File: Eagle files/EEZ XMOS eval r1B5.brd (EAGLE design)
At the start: 100 x 85 mm, 228 parts, among them IC1 TPS61169DCKR, IC10 IS42S16400J, IC11 SN74CBTLV3257, IC12 SN74LVC1G02DBVR, IC13 AT25SF041-SSHDT, IC14 SN74CBTLV3257, IC15 TPS2051BDBVR, IC16 TPD2E001DZDR, IC17 TPS561208DDCR, IC18 XE216-512-TQ128-C20, IC19 TPD4E001DRLR, IC2 TPS561208DDCR, IC20 TPD4E001DRLR, IC21 74LVC1G07SE-7, IC22 74LVC1G07SE-7, IC23 TPA6205A1DGN, IC24 DP83848CVV/NOPB, IC26 74VHC595MTC, IC27 PCA21125T/Q900/1,1, IC28 MCP23S17-E/SS, IC29 M95256-WMN6P, IC3 74VHC595MTC, IC4 TPS561208DDCR, IC5 74VHC595MTC, IC6 TPS3808G33DBVR, IC7 AR1021-I/SS, IC8 TPS3808G09DBVR, IC9 74AUP1G74DC.125, J1 678038020, J2 5033981892, Q1 IRLML2246TRPBF, SW1 1301.9316, X1 FC68149, X2 SSW-105-02-S-D, X3 TSW-104-02-S-D_NN, X4 TSW-103-07-F-D, X5 ZL231-20KG, X6 22-23-2021, X7 LMJTAB881243M-L, X8 SSW-107-02-S-D, X9 PCA-6G-20-HL-3 or 52746-2071, Y1 XTAL016178- 85SMX

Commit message: #1, #2
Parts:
- D1: value (none) -> NSR0240
- R13: device rcl:R1206 -> rcl:R0805
- R14, R24: value 10K -> 1K
- R23: value 56K -> 5K6
- R4: value 34K -> 15K
- R6: value 10K -> 4K7
- R67: value 0R -> N.C.
- R8: value 5K1 -> 2K7
- R9: value 16K -> 10K
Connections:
- removed net 3: X1.3
- net +3V3: now also X2.3
- net GND: now also X1.3; no longer X2.3
- net N$35: now also IC9.5; no longer IC9.3
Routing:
- net N$35: track 39.1 -> 36.1 mm
- net GND: track 258.5 -> 259.9 mm
- net N$78: track 2.72 -> 2.16 mm
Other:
- board text added: "(max."
- board text added: "16V)"
- board text added: "EEZ XMOS evaluation board (02/2018 r1B5)"
- board text removed: "(max. 16V)"
- board text removed: "EEZ XMOS evaluation board (01/2018 r1B4)"

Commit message: #3
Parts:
- removed ZD1: BZX384-B30.115, EEZ_Lib1:SOD323-W
- added C82: 2u2, rcl:C0805
- added JP1: 0R-JUMPA, jump-0r-smd:A0R-JMP
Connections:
- new net N$24: JP1.2, LCD1.36
- net !RESET: now also JP1.1; no longer LCD1.36
- net +3V3: now also C82.1
- net GND: now also C82.2, JP1.3
- net VLED+: no longer ZD1.C
- net VLED-: no longer ZD1.A
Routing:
- net N$24: track 0.00 -> 5.82 mm
- net !RESET: track 141.3 -> 136.3 mm
- net GND: track 259.9 -> 262.4 mm, vias 198 -> 200
- net +3V3: track 175.9 -> 178.2 mm
- net VLED-: track 15.0 -> 14.1 mm
- net VLED+: track 2.92 -> 3.82 mm
- net N$2: track 11.6 -> 10.9 mm
- net LCD_VSYNC: track 40.2 -> 39.4 mm

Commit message: fixed flash memory model
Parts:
- IC13: value AT25SF041-SSHDT -> AT25SF081-SSHDT
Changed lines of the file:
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@@
 <attribute name="NAME" x="50.975" y="74.1765" size="1.016" layer="25" ratio="10"/>
 </element>
-<element name="IC13" library="EEZ_Lib1" package="SOIC127P600X175-8N" value="AT25SF041-SSHDT" x="58.674" y="29.718" smashed="yes" rot="R270">
+<element name="IC13" library="EEZ_Lib1" package="SOIC127P600X175-8N" value="AT25SF081-SSHDT" x="58.674" y="29.718" smashed="yes" rot="R270">
 <attribute name="NAME" x="57.8866" y="33.528" size="1.016" layer="25" ratio="10" rot="SR0"/>
 <attribute name="VALUE" x="53.5686" y="29.337" size="0.6096" layer="27" ratio="10" rot="SR0"/>
@@
 </signal>
 </signals>
-<errors>
-</errors>
 </board>
 </drawing>

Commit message: #6
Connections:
- net !SPI0_TOUCH renamed !SPI1_TOUCH
- removed net N$4: C15.1, IC7.16, LCD1.38, R11.2
- new net N$53: C15.1, IC7.16, LCD1.38
- net +3V3: now also IC7.2
- net GND: now also IC7.4; no longer IC7.2
- net N$3: now also R11.2
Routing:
- net N$4: track 29.4 -> 0.00 mm, vias 3 -> 0
- net N$53: track 0.00 -> 19.7 mm, vias 0 -> 2
- net N$3: track 15.1 -> 23.1 mm, vias 0 -> 2
- net N$8: track 6.85 -> 7.50 mm
- net +3V3: track 178.2 -> 178.9 mm
- net !RESET: track 136.3 -> 135.7 mm
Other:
- board text added: "EEZ XMOS evaluation board (04/2018 r1B5)"
- board text removed: "EEZ XMOS evaluation board (02/2018 r1B5)"

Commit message: #7
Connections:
- net +3V3: now also R51.1, R52.1
- net GND: no longer R51.1, R52.1
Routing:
- net +3V3: track 178.9 -> 181.8 mm, vias 69 -> 70
- net GND: track 262.4 -> 259.5 mm, vias 200 -> 199
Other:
- board text added: "EEZ XMOS evaluation board (05/2018 r1B5)"
- board text removed: "EEZ XMOS evaluation board (04/2018 r1B5)"
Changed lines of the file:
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@@
 <layer number="21" name="tPlace" color="7" fill="1" visible="yes" active="yes"/>
 <layer number="22" name="bPlace" color="3" fill="1" visible="no" active="yes"/>
-<layer number="23" name="tOrigins" color="15" fill="1" visible="no" active="yes"/>
+<layer number="23" name="tOrigins" color="15" fill="1" visible="yes" active="yes"/>
 <layer number="24" name="bOrigins" color="15" fill="1" visible="no" active="yes"/>
 <layer number="25" name="tNames" color="7" fill="1" visible="yes" active="yes"/>
@@
 <rectangle x1="95.9784" y1="77.4253" x2="96.3784" y2="77.4291" layer="21"/>
 <rectangle x1="96.0317" y1="77.4291" x2="96.2717" y2="77.4329" layer="21"/>
-<text x="99.1275" y="15.2085" size="1.016" layer="21" font="vector" ratio="10" rot="SR90">EEZ XMOS evaluation board (04/2018 r1B5)</text>
-<text x="1.5875" y="23.241" size="1.016" layer="16" ratio="10" rot="SMR90">EEZ XMOS evaluation board (04/2018 r1B5)</text>
+<text x="99.1275" y="15.2085" size="1.016" layer="21" font="vector" ratio="10" rot="SR90">EEZ XMOS evaluation board (05/2018 r1B5)</text>
+<text x="1.5875" y="23.241" size="1.016" layer="16" ratio="10" rot="SMR90">EEZ XMOS evaluation board (05/2018 r1B5)</text>
 <wire x1="100" y1="83.5" x2="100" y2="1.5" width="0.1" layer="20"/>
 <dimension x1="0" y1="-2" x2="100" y2="-3.5" x3="50" y3="-7" layer="47" dtype="horizontal"/>
@@
 <contactref element="C71" pad="-"/>
 <contactref element="C72" pad="2"/>
-<contactref element="R52" pad="1"/>
-<contactref element="R51" pad="1"/>
 <contactref element="IC24" pad="35"/>
 <contactref element="IC24" pad="47"/>
@@
 <wire x1="56.0705" y1="63.6905" x2="56.8842" y2="63.881" width="0.2032" layer="1"/>
 <wire x1="56.8842" y1="63.881" x2="56.9096" y2="63.8556" width="0.2032" layer="1"/>
-<via x="73.406" y="73.152" extent="1-16" drill="0.3" shape="square"/>
 <via x="55.372" y="58.674" extent="1-16" drill="0.3" shape="square"/>
 <wire x1="64.262" y1="69.472" x2="64.262" y2="70.5485" width="0.254" layer="1"/>
@@
 <wire x1="59.563" y1="53.975" x2="59.563" y2="53.2647" width="0.254" layer="1"/>
 <wire x1="59.563" y1="53.2647" x2="59.5766" y2="53.2511" width="0.254" layer="1"/>
-<wire x1="71.4629" y1="72.2351" x2="73.4314" y2="72.2351" width="0.254" layer="1"/>
-<wire x1="73.4314" y1="72.2351" x2="73.4314" y2="73.1266" width="0.254" layer="1"/>
-<wire x1="73.4314" y1="73.1266" x2="73.406" y2="73.152" width="0.254" layer="1"/>
 <wire x1="79.7179" y1="65.9756" x2="79.7179" y2="66.7766" width="0.254" layer="1"/>
 <wire x1="79.7179" y1="66.7766" x2="79.6925" y2="66.802" width="0.254" layer="1"/>
@@
 <wire x1="41.099" y1="8.2695" x2="41.11625" y2="8.28675" width="0.4064" layer="1"/>
 <contactref element="IC7" pad="4"/>
+<wire x1="47.8282" y1="15.2527" x2="48.4886" y2="15.2527" width="0.1524" layer="1"/>
 <wire x1="69.596" y1="13.7795" x2="69.6415" y2="13.7795" width="0" layer="19" extent="1-1"/>
 <wire x1="8.3185" y1="7.369" x2="8.3185" y2="7.366" width="0" layer="19" extent="1-1"/>
-<wire x1="47.8282" y1="15.2527" x2="48.4886" y2="15.2527" width="0.1524" layer="1"/>
 </signal>
 <signal name="HOLE_UL">
@@
 <contactref element="IC7" pad="2"/>
 <wire x1="49.149" y1="15.2527" x2="49.784" y2="15.2527" width="0.1524" layer="1"/>
+<contactref element="R52" pad="1"/>
+<contactref element="R51" pad="1"/>
+<via x="73.406" y="73.152" extent="1-16" drill="0.3" shape="octagon"/>
+<wire x1="71.4629" y1="72.2351" x2="73.4314" y2="72.2351" width="0.254" layer="1"/>
+<wire x1="73.4314" y1="72.2351" x2="73.4314" y2="73.1266" width="0.254" layer="1"/>
+<wire x1="73.4314" y1="73.1266" x2="73.406" y2="73.152" width="0.254" layer="1"/>
 </signal>
 <signal name="N$28">

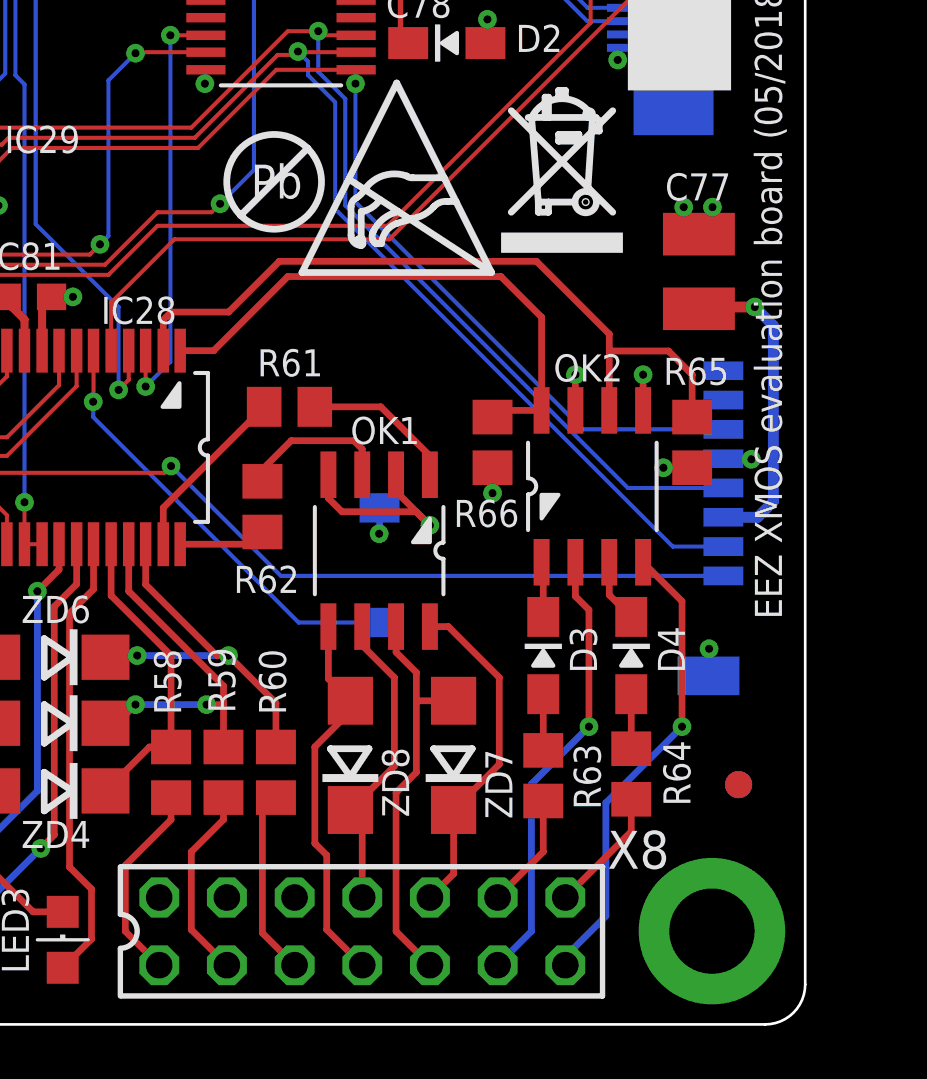
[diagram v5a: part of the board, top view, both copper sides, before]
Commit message: better placement of SD card capacitor (C77)
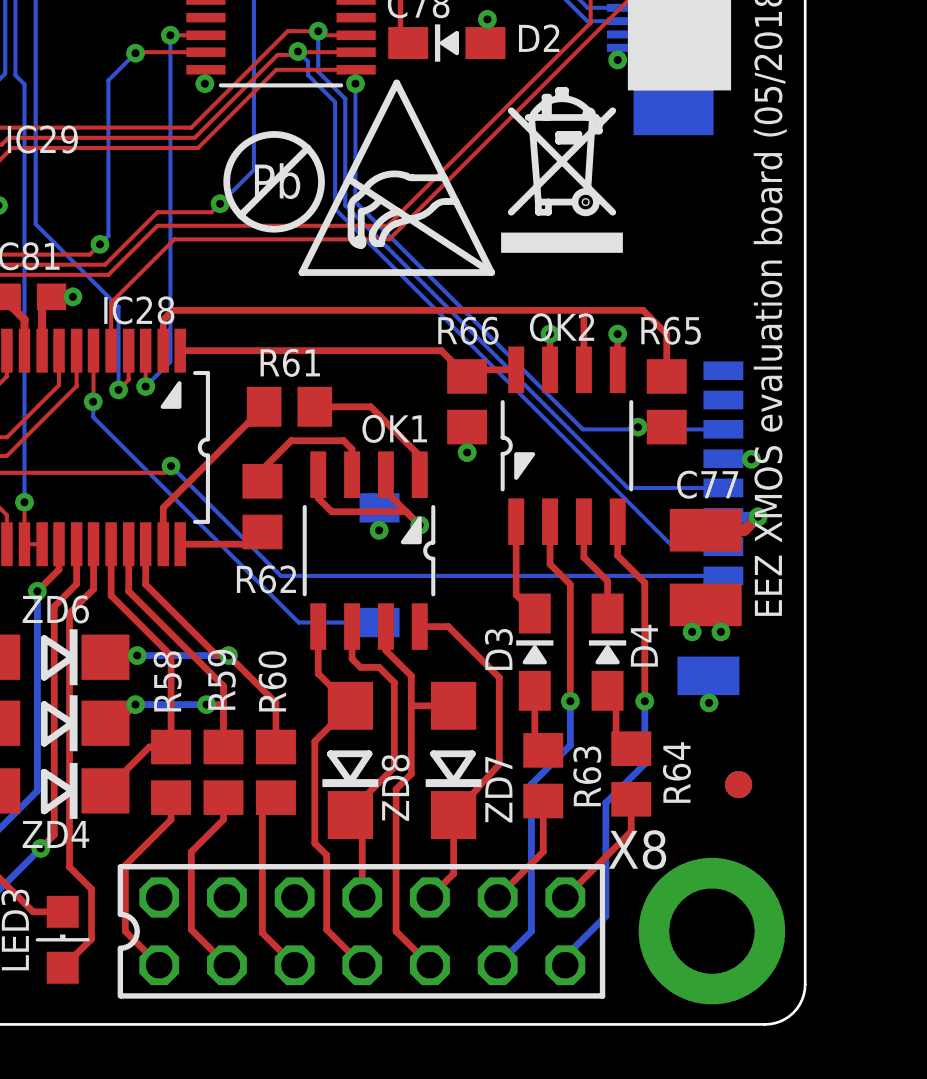
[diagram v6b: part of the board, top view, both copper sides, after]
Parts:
- moved C77 11.1 mm to (96.3, 17.1), turned to 270 degrees
- moved OK2 1.80 mm to (91.1, 21.7)
- moved R65 1.80 mm to (94.8, 23.4)
- moved R66 1.80 mm to (87.3, 23.4)
- moved D4 0.90 mm to (92.6, 14.0)
- moved OK1 0.38 mm to (83.6, 17.8)
- moved D3 0.34 mm to (89.9, 14.0)
- moved ZD7 0.19 mm to (86.8, 9.91)
- moved ZD8 0.19 mm to (82.9, 9.91)
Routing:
- net IOEXP_OCI1: track 20.8 -> 13.1 mm
- net +3V3: track 181.8 -> 175.6 mm
- net IOEXP_OCI2: track 27.9 -> 24.4 mm
- net N$29: track 2.08 -> 3.74 mm
- net N$45: track 2.39 -> 3.82 mm
- net N$38: track 16.8 -> 18.1 mm
- net N$44: track 2.04 -> 2.84 mm
- net N$25: track 11.5 -> 12.2 mm

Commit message: #8
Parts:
- moved C77 0.83 mm to (96.3, 18.0)
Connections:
- net !SPI1_SDCARD: now also J2.2; no longer J2.1
- net +3V3: now also J2.4; no longer J2.3
- net GND: now also J2.6; no longer J2.5
- net SPI1_CLK: now also J2.5; no longer J2.4
- net SPI1_MISO: now also J2.7; no longer J2.6
- net SPI1_MOSI: now also J2.3; no longer J2.2
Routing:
- net GND: track 259.8 -> 258.3 mm
- net +3V3: track 175.6 -> 174.9 mm
